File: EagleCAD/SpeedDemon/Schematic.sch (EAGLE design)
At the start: 72 parts, among them Q1 DMC2700, U3 LM3676, U4 STM32F072-LQFP48, X1 32.768kHz

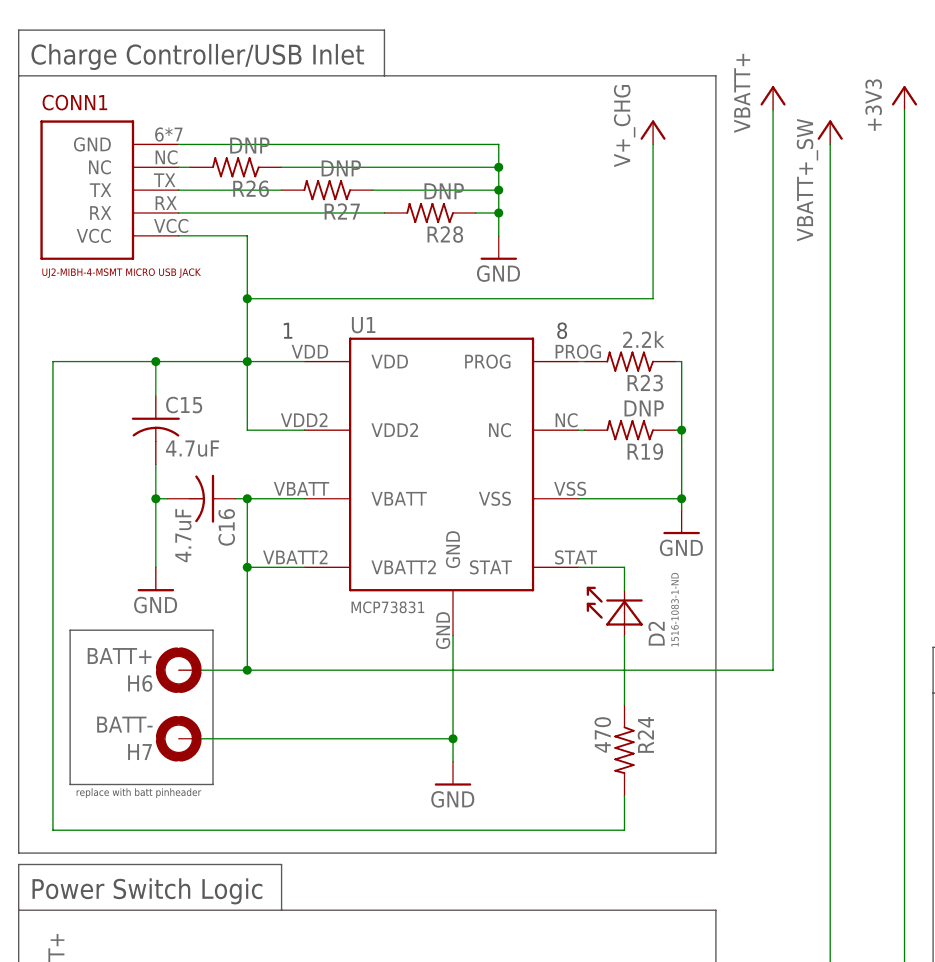
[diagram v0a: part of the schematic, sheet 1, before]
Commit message: Updated battery connector.
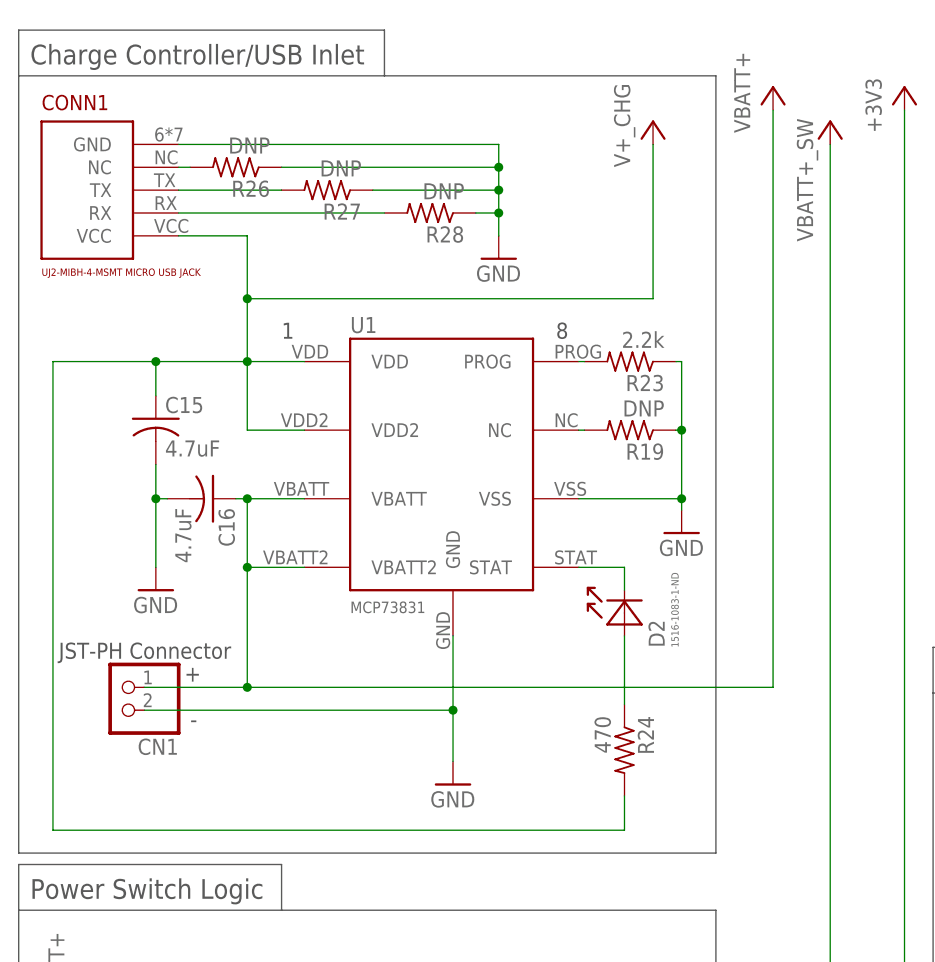
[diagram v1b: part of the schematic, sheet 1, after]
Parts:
- removed H6: BATT+, holes:MOUNT-PAD-ROUND3.6
- removed H7: BATT-, holes:MOUNT-PAD-ROUND3.6
- added CN1: (no value), adafruit:JST_2PIN-SMT-RA
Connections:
- net GND: now also CN1.1; no longer H7.MOUNT
- net VBATT+: now also CN1.2; no longer H6.MOUNT
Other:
- note added: "+"
- note added: "-"
- note added: "JST-PH Connector"
- note removed: "replace with batt pinheader"
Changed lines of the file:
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@@
 <?xml version="1.0" encoding="utf-8"?>
 <!DOCTYPE eagle SYSTEM "eagle.dtd">
-<eagle version="8.4.0">
+<eagle version="8.4.1">
 <drawing>
 <settings>
@@
 <part name="+3V8" library="supply1" library_urn="urn:adsk.eagle:library:371" deviceset="+3V3" device=""/>
 <part name="U3" library="LM3676" deviceset="LM3676" device=""/>
-<part name="H6" library="holes" library_urn="urn:adsk.eagle:library:237" deviceset="MOUNT-PAD-ROUND" device="3.6" package3d_urn="urn:adsk.eagle:package:14284/1" value="BATT+"/>
-<part name="H7" library="holes" library_urn="urn:adsk.eagle:library:237" deviceset="MOUNT-PAD-ROUND" device="3.6" package3d_urn="urn:adsk.eagle:package:14284/1" value="BATT-"/>
 <part name="+3V9" library="supply1" library_urn="urn:adsk.eagle:library:371" deviceset="+3V3" device=""/>
 <part name="+3V10" library="supply1" library_urn="urn:adsk.eagle:library:371" deviceset="+3V3" device=""/>
@@
 <part name="X1" library="LCRD_SMD_generics" deviceset="XC2292CT-ND" device="" value="32.768kHz"/>
 <part name="JP5" library="pinhead" library_urn="urn:adsk.eagle:library:325" deviceset="PINHD-1X3" device="" package3d_urn="urn:adsk.eagle:package:22458/2"/>
+<part name="CN1" library="adafruit" library_urn="urn:adsk.eagle:library:420" deviceset="JST_2PIN" device="-SMT-RA"/>
 </parts>
 <sheets>
@@
 <text x="119.38" y="76.2" size="0.8128" layer="97">Chip clock runs on x8 freq multiplication</text>
 <text x="218.44" y="21.59" size="0.8128" layer="97" rot="R90">See p.2 for switch connections</text>
-<wire x1="29.21" y1="186.055" x2="29.21" y2="168.91" width="0.1524" layer="97"/>
-<wire x1="29.21" y1="168.91" x2="13.335" y2="168.91" width="0.1524" layer="97"/>
-<wire x1="13.335" y1="168.91" x2="13.335" y2="186.055" width="0.1524" layer="97"/>
-<wire x1="13.335" y1="186.055" x2="29.21" y2="186.055" width="0.1524" layer="97"/>
-<text x="13.97" y="167.64" size="0.8128" layer="97">replace with batt pinheader</text>
+<text x="26.035" y="180.34" size="1.778" layer="97">+</text>
+<text x="26.67" y="175.26" size="1.778" layer="97">-</text>
+<text x="12.065" y="182.88" size="1.778" layer="97">JST-PH Connector</text>
 </plain>
 <instances>
@@
 <instance part="+3V8" gate="G$1" x="158.75" y="177.8"/>
 <instance part="U3" gate="G$1" x="43.18" y="27.94"/>
-<instance part="H6" gate="G$1" x="25.4" y="181.61" rot="R180"/>
-<instance part="H7" gate="G$1" x="25.4" y="173.99" rot="R180"/>
 <instance part="+3V9" gate="G$1" x="307.34" y="85.09"/>
 <instance part="+3V10" gate="G$1" x="370.84" y="77.47"/>
@@
 <instance part="X1" gate="G$1" x="132.08" y="91.44" rot="R90"/>
 <instance part="JP5" gate="A" x="117.475" y="41.91" rot="R180"/>
+<instance part="CN1" gate="G$1" x="19.05" y="179.705" rot="R180"/>
 </instances>
 <busses>
@@
 <pinref part="U1" gate="G$1" pin="GND"/>
 <pinref part="GND19" gate="1" pin="GND"/>
-<wire x1="55.88" y1="185.42" x2="55.88" y2="173.99" width="0.1524" layer="91"/>
-<pinref part="H7" gate="G$1" pin="MOUNT"/>
-<wire x1="55.88" y1="173.99" x2="55.88" y2="171.45" width="0.1524" layer="91"/>
-<wire x1="55.88" y1="173.99" x2="27.94" y2="173.99" width="0.1524" layer="91"/>
-<junction x="55.88" y="173.99"/>
+<wire x1="55.88" y1="185.42" x2="55.88" y2="177.165" width="0.1524" layer="91"/>
+<wire x1="55.88" y1="177.165" x2="55.88" y2="171.45" width="0.1524" layer="91"/>
+<wire x1="21.59" y1="177.165" x2="55.88" y2="177.165" width="0.1524" layer="91"/>
+<junction x="55.88" y="177.165"/>
+<pinref part="CN1" gate="G$1" pin="1"/>
 </segment>
 <segment>
@@
 </segment>
 <segment>
+<wire x1="91.44" y1="179.705" x2="91.44" y2="243.84" width="0.1524" layer="91"/>
+<pinref part="VBATT+2" gate="G$1" pin="VBATT+"/>
+<pinref part="CN1" gate="G$1" pin="2"/>
+<wire x1="21.59" y1="179.705" x2="33.02" y2="179.705" width="0.1524" layer="91"/>
+<pinref part="C16" gate="G$1" pin="1"/>
+<pinref part="U1" gate="G$1" pin="VBATT"/>
+<wire x1="33.02" y1="200.66" x2="39.37" y2="200.66" width="0.1524" layer="91"/>
+<wire x1="33.02" y1="200.66" x2="31.75" y2="200.66" width="0.1524" layer="91"/>
+<junction x="33.02" y="200.66"/>
 <pinref part="U1" gate="G$1" pin="VBATT2"/>
 <wire x1="39.37" y1="193.04" x2="33.02" y2="193.04" width="0.1524" layer="91"/>
 <wire x1="33.02" y1="193.04" x2="33.02" y2="200.66" width="0.1524" layer="91"/>
-<pinref part="U1" gate="G$1" pin="VBATT"/>
-<wire x1="33.02" y1="200.66" x2="39.37" y2="200.66" width="0.1524" layer="91"/>
-<pinref part="C16" gate="G$1" pin="1"/>
-<wire x1="33.02" y1="200.66" x2="31.75" y2="200.66" width="0.1524" layer="91"/>
-<junction x="33.02" y="200.66"/>
-<pinref part="H6" gate="G$1" pin="MOUNT"/>
-<wire x1="27.94" y1="181.61" x2="33.02" y2="181.61" width="0.1524" layer="91"/>
-<wire x1="33.02" y1="181.61" x2="33.02" y2="193.04" width="0.1524" layer="91"/>
 <junction x="33.02" y="193.04"/>
-<wire x1="33.02" y1="181.61" x2="91.44" y2="181.61" width="0.1524" layer="91"/>
-<wire x1="91.44" y1="181.61" x2="91.44" y2="243.84" width="0.1524" layer="91"/>
-<junction x="33.02" y="181.61"/>
-<pinref part="VBATT+2" gate="G$1" pin="VBATT+"/>
-</segment>
-<segment>
+<wire x1="33.02" y1="179.705" x2="33.02" y2="193.04" width="0.1524" layer="91"/>
+<wire x1="33.02" y1="179.705" x2="91.44" y2="179.705" width="0.1524" layer="91"/>
+<junction x="33.02" y="179.705"/>
+</segment>
+<segment>

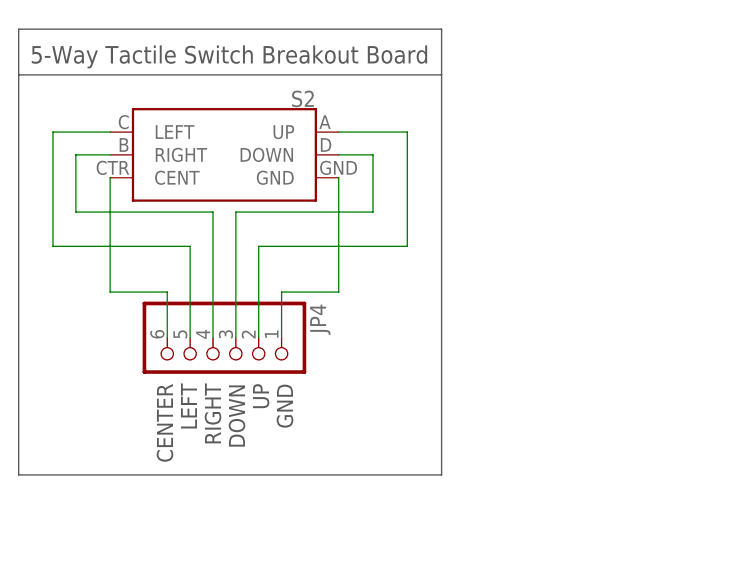
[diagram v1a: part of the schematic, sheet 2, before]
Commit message: Started a board layout
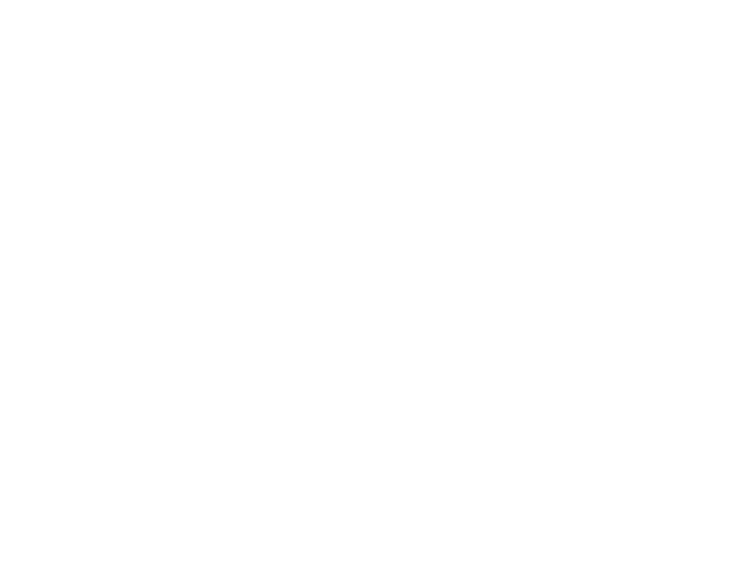
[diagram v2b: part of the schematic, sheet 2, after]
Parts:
- removed JP4: (no value), pinhead:PINHD-1X6
- removed R2: 10k, rcl:R-US_R0805
- removed R6: 0, rcl:R-US_R0805
- removed S1: MOMENTARY-SWITCH-SPST-PTH-6.0MM, SparkFun-Switches:MOMENTARY-SWITCH-SPST-PTH-6.0MM
- removed S2: (no value), SparkFun-Switches:JOYSTICK_MINI
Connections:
- removed net N$4: R2.2, S1.1
- removed net N$8: R1.1, R2.1, R6.2
- removed net SW_CTR_CARD: JP4.6, S2.CENT
- removed net SW_DN_CARD: JP4.3, S2.DOWN
- removed net SW_GND_CARD: JP4.1, S2.GND
- removed net SW_LEFT_CARD: JP4.5, S2.LEFT
- removed net SW_RIGHT_CARD: JP4.4, S2.RIGHT
- removed net SW_UP_CARD: JP4.2, S2.UP
- net FL_RESET: now also R1.1; no longer R6.1
- net GND: no longer S1.2
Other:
- note removed: "5-Way Tactile Switch Breakout Board"
- note removed: "This is a 4-pin push button. We can update this when we decide on a button we want to use."
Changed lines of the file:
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@@
 <part name="JP1" library="pinhead" library_urn="urn:adsk.eagle:library:325" deviceset="PINHD-2X5" device="" package3d_urn="urn:adsk.eagle:package:22470/2"/>
 <part name="R1" library="rcl" library_urn="urn:adsk.eagle:library:334" deviceset="R-US_" device="R0805" package3d_urn="urn:adsk.eagle:package:23553/2" value="0"/>
-<part name="R2" library="rcl" library_urn="urn:adsk.eagle:library:334" deviceset="R-US_" device="R0805" package3d_urn="urn:adsk.eagle:package:23553/2" value="10k"/>
 <part name="R3" library="rcl" library_urn="urn:adsk.eagle:library:334" deviceset="R-US_" device="R0805" package3d_urn="urn:adsk.eagle:package:23553/2" value="10k"/>
 <part name="R4" library="rcl" library_urn="urn:adsk.eagle:library:334" deviceset="R-US_" device="R0805" package3d_urn="urn:adsk.eagle:package:23553/2" value="10k"/>
-<part name="R6" library="rcl" library_urn="urn:adsk.eagle:library:334" deviceset="R-US_" device="R0805" package3d_urn="urn:adsk.eagle:package:23553/2" value="0"/>
 <part name="R7" library="rcl" library_urn="urn:adsk.eagle:library:334" deviceset="R-US_" device="R0805" package3d_urn="urn:adsk.eagle:package:23553/2" value="22"/>
 <part name="R8" library="rcl" library_urn="urn:adsk.eagle:library:334" deviceset="R-US_" device="R0805" package3d_urn="urn:adsk.eagle:package:23553/2" value="10k"/>
 <part name="R9" library="rcl" library_urn="urn:adsk.eagle:library:334" deviceset="R-US_" device="R0805" package3d_urn="urn:adsk.eagle:package:23553/2" value="10k"/>
-<part name="S1" library="SparkFun-Switches" library_urn="urn:adsk.eagle:library:535" deviceset="MOMENTARY-SWITCH-SPST" device="-PTH-6.0MM" package3d_urn="urn:adsk.eagle:package:40163/1"/>
-<part name="GND1" library="supply1" library_urn="urn:adsk.eagle:library:371" deviceset="GND" device=""/>
 <part name="+3V1" library="supply1" library_urn="urn:adsk.eagle:library:371" deviceset="+3V3" device=""/>
 <part name="P+1" library="supply1" library_urn="urn:adsk.eagle:library:371" deviceset="+5V" device=""/>
@@
 <part name="GND8" library="supply1" library_urn="urn:adsk.eagle:library:371" deviceset="GND" device=""/>
 <part name="JP3" library="pinhead" library_urn="urn:adsk.eagle:library:325" deviceset="PINHD-1X6" device="" package3d_urn="urn:adsk.eagle:package:22472/2"/>
-<part name="JP4" library="pinhead" library_urn="urn:adsk.eagle:library:325" deviceset="PINHD-1X6" device="" package3d_urn="urn:adsk.eagle:package:22472/2"/>
-<part name="S2" library="SparkFun-Switches" library_urn="urn:adsk.eagle:library:535" deviceset="JOYSTICK_MINI" device="" package3d_urn="urn:adsk.eagle:package:40157/1"/>
 <part name="R5" library="rcl" library_urn="urn:adsk.eagle:library:334" deviceset="R-US_" device="R0805" package3d_urn="urn:adsk.eagle:package:23553/2" value="0"/>
 <part name="X1" library="LCRD_SMD_generics" deviceset="XC2292CT-ND" device="" value="32.768kHz"/>
@@
 <wire x1="381" y1="248.92" x2="337.82" y2="248.92" width="0.1524" layer="97"/>
 <text x="267.97" y="250.19" size="2.1844" layer="97">Pinheader for  Serial Wire Debug (SWD) interface.</text>
-<text x="322.58" y="238.76" size="1.778" layer="97">This is a 4-pin push button. We can update
-this when we decide on a button we want to use.</text>
 <text x="35.56" y="180.34" size="1.778" layer="91"></text>
 <wire x1="7.62" y1="7.62" x2="7.62" y2="57.15" width="0.1524" layer="97"/>
@@
 <instance part="JP1" gate="A" x="335.28" y="218.44"/>
 <instance part="R1" gate="G$1" x="320.04" y="223.52"/>
-<instance part="R2" gate="G$1" x="312.42" y="228.6" rot="R90"/>
 <instance part="R3" gate="G$1" x="297.18" y="236.22" rot="R90"/>
 <instance part="R4" gate="G$1" x="289.56" y="236.22" rot="R90"/>
-<instance part="R6" gate="G$1" x="304.8" y="223.52"/>
 <instance part="R7" gate="G$1" x="360.68" y="213.36" rot="R90"/>
 <instance part="R8" gate="G$1" x="274.32" y="236.22" rot="R90"/>
 <instance part="R9" gate="G$1" x="281.94" y="236.22" rot="R90"/>
-<instance part="S1" gate="G$1" x="342.9" y="233.68"/>
-<instance part="GND1" gate="1" x="373.38" y="228.6"/>
 <instance part="+3V1" gate="G$1" x="297.18" y="246.38"/>
 <instance part="P+1" gate="1" x="289.56" y="246.38"/>
@@
 <net name="FL_RESET" class="0">
 <segment>
-<wire x1="262.89" y1="223.52" x2="299.72" y2="223.52" width="0.1524" layer="91"/>
-<pinref part="R6" gate="G$1" pin="1"/>
+<wire x1="262.89" y1="223.52" x2="314.96" y2="223.52" width="0.1524" layer="91"/>
 <label x="251.46" y="222.25" size="1.778" layer="95"/>
+<pinref part="R1" gate="G$1" pin="1"/>
 </segment>
 <segment>
@@
 <wire x1="162.56" y1="127" x2="157.48" y2="127" width="0.1524" layer="91"/>
 <label x="149.225" y="126.365" size="1.27" layer="95"/>
-</segment>
-</net>
-<net name="N$4" class="0">
-<segment>
-<pinref part="R2" gate="G$1" pin="2"/>
-<wire x1="312.42" y1="233.68" x2="337.82" y2="233.68" width="0.1524" layer="91"/>
-<pinref part="S1" gate="G$1" pin="1"/>
 </segment>
 </net>
@@
 </segment>
 </net>
-<net name="N$8" class="0">
-<segment>
-<pinref part="R1" gate="G$1" pin="1"/>
-<pinref part="R2" gate="G$1" pin="1"/>
-<wire x1="314.96" y1="223.52" x2="312.42" y2="223.52" width="0.1524" layer="91"/>
-<pinref part="R6" gate="G$1" pin="2"/>
-<wire x1="312.42" y1="223.52" x2="309.88" y2="223.52" width="0.1524" layer="91"/>
-<junction x="312.42" y="223.52"/>
-</segment>
-</net>
 <net name="N$9" class="0">
 <segment>
@@
 </net>
 <net name="GND" class="0">
-<segment>
-<pinref part="S1" gate="G$1" pin="2"/>
-<wire x1="373.38" y1="233.68" x2="347.98" y2="233.68" width="0.1524" layer="91"/>
-<pinref part="GND1" gate="1" pin="GND"/>
-<wire x1="373.38" y1="231.14" x2="373.38" y2="233.68" width="0.1524" layer="91"/>
-</segment>
 <segment>
 <pinref part="GND2" gate="1" pin="GND"/>
@@
 (tie gnd to cable shield)</text>
 <text x="98.425" y="253.365" size="1.6764" layer="97">*NOTE: No PCB for this portion of circuit! Use point-to-point wiring.</text>
-<wire x1="5.715" y1="249.555" x2="52.705" y2="249.555" width="0.1524" layer="97"/>
-<wire x1="52.705" y1="249.555" x2="52.705" y2="205.105" width="0.1524" layer="97"/>
-<wire x1="52.705" y1="205.105" x2="5.715" y2="205.105" width="0.1524" layer="97"/>
-<wire x1="5.715" y1="205.105" x2="5.715" y2="249.555" width="0.1524" layer="97"/>
-<text x="6.985" y="250.825" size="1.9304" layer="97">5-Way Tactile Switch Breakout Board</text>
-<wire x1="5.715" y1="249.555" x2="5.715" y2="254.635" width="0.1524" layer="97"/>
-<wire x1="5.715" y1="254.635" x2="52.705" y2="254.635" width="0.1524" layer="97"/>
-<wire x1="52.705" y1="254.635" x2="52.705" y2="249.555" width="0.1524" layer="97"/>
-<text x="36.195" y="215.265" size="1.778" layer="97" rot="R90" align="bottom-right">CENTER
-LEFT
-RIGHT
-DOWN
-UP
-GND</text>
 </plain>
 <instances>
@@
 <instance part="U1A" gate="G$1" x="111.125" y="220.98"/>
 <instance part="FRAME2" gate="G$1" x="0" y="0"/>
-<instance part="JP4" gate="A" x="27.305" y="217.805" rot="R270"/>
-<instance part="S2" gate="G$1" x="28.575" y="240.665" rot="MR0"/>
 </instances>
 <busses>
@@
 </segment>
 </net>
-<net name="SW_CTR_CARD" class="0">
-<segment>
-<pinref part="S2" gate="G$1" pin="CENT"/>
-<wire x1="15.875" y1="238.125" x2="15.875" y2="225.425" width="0.1524" layer="91"/>
-<wire x1="15.875" y1="225.425" x2="22.225" y2="225.425" width="0.1524" layer="91"/>
-<pinref part="JP4" gate="A" pin="6"/>
-<wire x1="22.225" y1="225.425" x2="22.225" y2="220.345" width="0.1524" layer="91"/>
-</segment>
-</net>
-<net name="SW_GND_CARD" class="0">
-<segment>
-<pinref part="S2" gate="G$1" pin="GND"/>
-<wire x1="41.275" y1="238.125" x2="41.275" y2="225.425" width="0.1524" layer="91"/>
-<wire x1="41.275" y1="225.425" x2="34.925" y2="225.425" width="0.1524" layer="91"/>
-<wire x1="34.925" y1="225.425" x2="34.925" y2="220.345" width="0.1524" layer="91"/>
-<pinref part="JP4" gate="A" pin="1"/>
-</segment>
-</net>
-<net name="SW_RIGHT_CARD" class="0">
-<segment>
-<pinref part="S2" gate="G$1" pin="RIGHT"/>
-<wire x1="15.875" y1="240.665" x2="12.065" y2="240.665" width="0.1524" layer="91"/>
-<wire x1="12.065" y1="240.665" x2="12.065" y2="234.315" width="0.1524" layer="91"/>
-<wire x1="12.065" y1="234.315" x2="27.305" y2="234.315" width="0.1524" layer="91"/>
-<pinref part="JP4" gate="A" pin="4"/>
-<wire x1="27.305" y1="234.315" x2="27.305" y2="220.345" width="0.1524" layer="91"/>
-</segment>
-</net>
-<net name="SW_LEFT_CARD" class="0">
-<segment>
-<pinref part="S2" gate="G$1" pin="LEFT"/>
-<wire x1="15.875" y1="243.205" x2="9.525" y2="243.205" width="0.1524" layer="91"/>
-<wire x1="9.525" y1="243.205" x2="9.525" y2="230.505" width="0.1524" layer="91"/>
-<wire x1="9.525" y1="230.505" x2="24.765" y2="230.505" width="0.1524" layer="91"/>
-<pinref part="JP4" gate="A" pin="5"/>
-<wire x1="24.765" y1="230.505" x2="24.765" y2="220.345" width="0.1524" layer="91"/>
-</segment>
-</net>
-<net name="SW_DN_CARD" class="0">
-<segment>
-<pinref part="JP4" gate="A" pin="3"/>
-<wire x1="29.845" y1="220.345" x2="29.845" y2="234.315" width="0.1524" layer="91"/>
-<wire x1="29.845" y1="234.315" x2="45.085" y2="234.315" width="0.1524" layer="91"/>
-<wire x1="45.085" y1="234.315" x2="45.085" y2="240.665" width="0.1524" layer="91"/>
-<pinref part="S2" gate="G$1" pin="DOWN"/>
-<wire x1="45.085" y1="240.665" x2="41.275" y2="240.665" width="0.1524" layer="91"/>
-</segment>
-</net>
-<net name="SW_UP_CARD" class="0">
-<segment>
-<wire x1="32.385" y1="220.345" x2="32.385" y2="230.505" width="0.1524" layer="91"/>
-<wire x1="32.385" y1="230.505" x2="48.895" y2="230.505" width="0.1524" layer="91"/>
-<pinref part="S2" gate="G$1" pin="UP"/>
-<wire x1="48.895" y1="230.505" x2="48.895" y2="243.205" width="0.1524" layer="91"/>
-<wire x1="48.895" y1="243.205" x2="41.275" y2="243.205" width="0.1524" layer="91"/>
-<pinref part="JP4" gate="A" pin="2"/>
-</segment>
-</net>

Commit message: board layout.. needs some work
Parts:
- added C19: 1uF, 0805_generics:C_0805_NP
- added C20: 100nF, 0805_generics:C_0805_NP
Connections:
- net +3V3: now also C19.1, C20.1
- net GND: now also C19.2, C20.2, U4.BOOT0(P44), U4.PA0/USART4_TX/WKUP1/ADC_IN0, U4.PA1/ADC_IN1/COMP1_INP/USART4_RX, U4.PA10/USART1_RX/TIM1_CH3, U4.PA11/USB_DM/CAN_RX, U4.PA12/USB_DP/CAN_TX, U4.PA15/USART2_RX, U4.PA2/ADC_IN2/WKUP4USART2_TX, U4.PA8/TIM1_CH1, U4.PA9/USART1_TX/TIM1_CH2, U4.PB14/SPI2_MISO/I2C2_SDA, U4.PB15/WKUP7/RTC_REFIN/SPI2_MOSI, U4.PB6USART1_TX/I2C1_SCL, U4.PB8/I2C1_SCL/TIM16_CH1/CAN_RX, U4.PB9/I2C1_SDA/TIM17_CH1/CAN_TX, U4.PC13/WKUP2/RTC_TAMP1/RTC_TS/RTC_OUT, U4.PF0/OSC_IN, U4.PF1/OSC_OUT
